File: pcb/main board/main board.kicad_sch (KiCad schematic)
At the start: 33 parts, among them J10 12V Battery, J11 BAU, J12 Servo 4 Conn, J13 Servo 1 Conn, J14 Servo 2 Conn, J15 Servo 3 Conn, J16 Servo 5 Conn, J17 Servo 6 Conn, J5 I2C 0 Conn, J6 I2C 1 Conn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

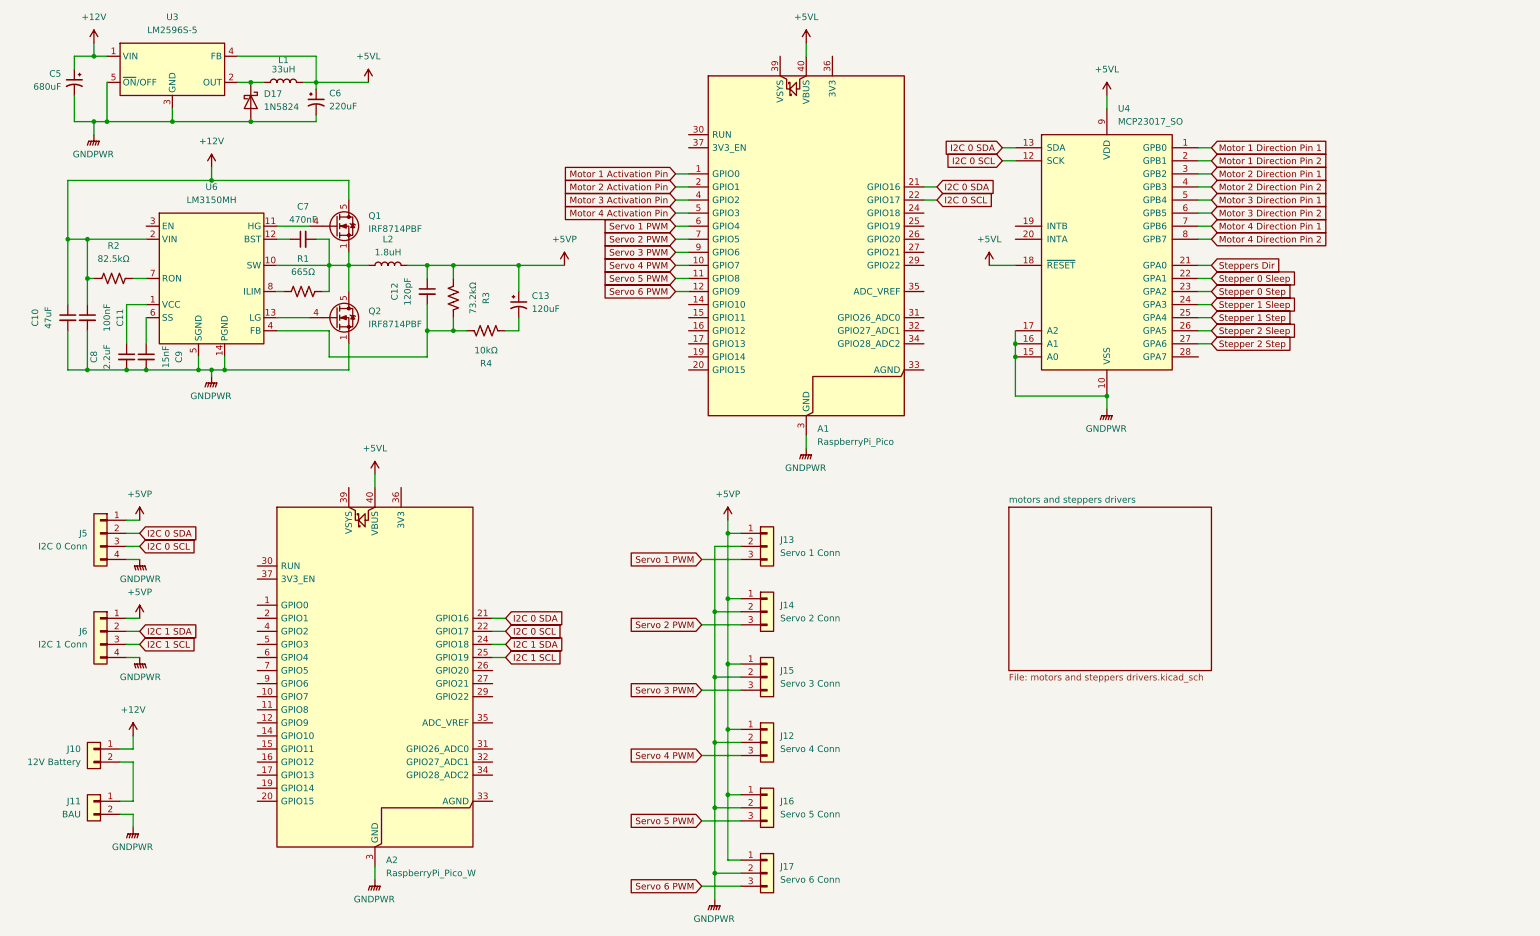
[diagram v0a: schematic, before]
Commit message: Modified LM2596S to be a module.
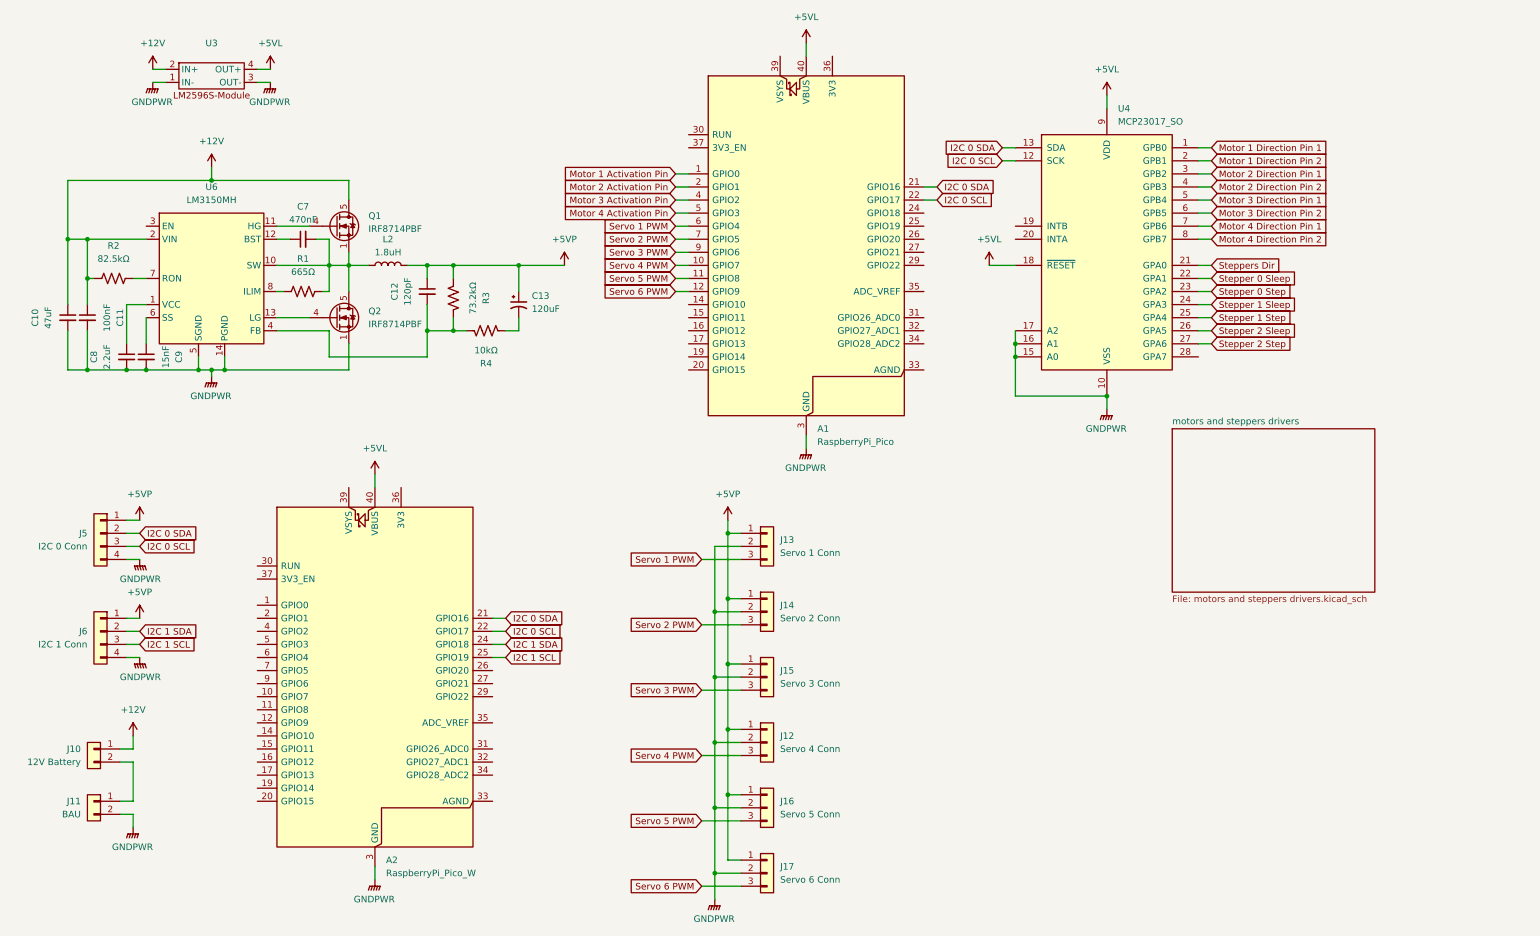
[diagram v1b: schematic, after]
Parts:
- removed C5: 680uF, symbol Device:C_Polarized_Small_US
- removed C6: 220uF, symbol Device:C_Polarized_Small_US
- removed D17: 1N5824, Diode_THT:D_DO-201AD_P15.24mm_Horizontal, symbol Diode:1N5822
- removed L1: 33uH, symbol Device:L
- removed U3: LM2596S-5, Package_TO_SOT_SMD:TO-263-5_TabPin3, symbol Regulator_Switching:LM2596S-5
- added U3: ~, LM2596S-Module:LM2596S-Module, symbol LM2596S-Module:LM2596S-Module
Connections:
- net +12V: now also U3.2 (IN+)
- net +5VL: now also U3.4 (OUT+)
- net GNDPWR: now also U3.1 (IN-), U3.3 (OUT-)

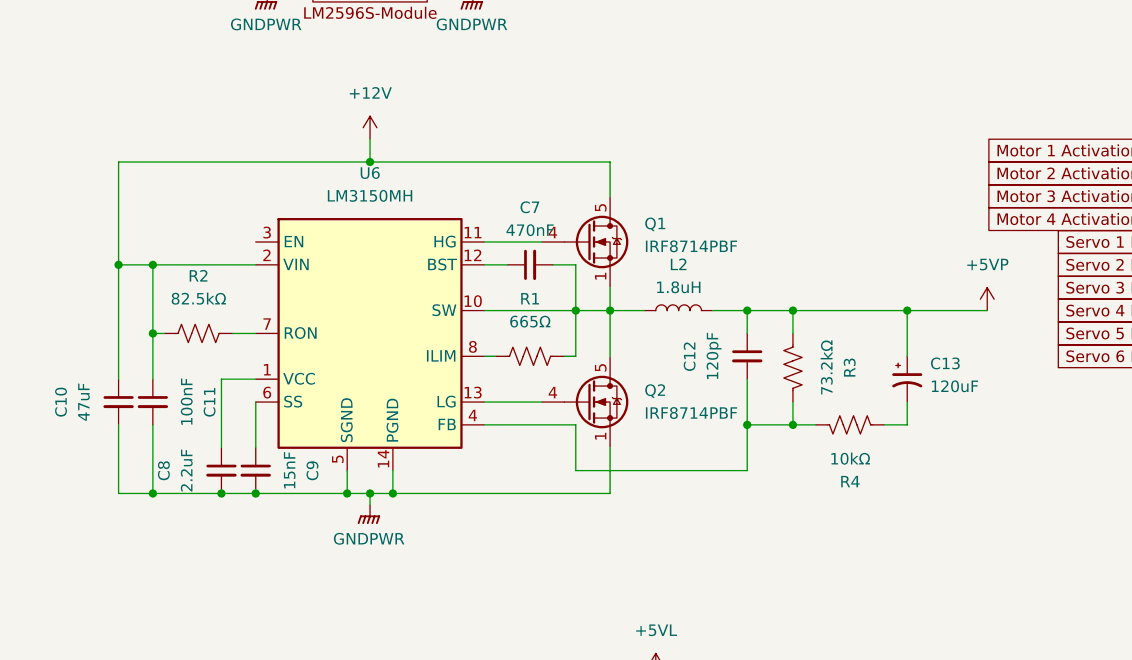
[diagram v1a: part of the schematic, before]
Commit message: Changed some capacitors and assigned every component.
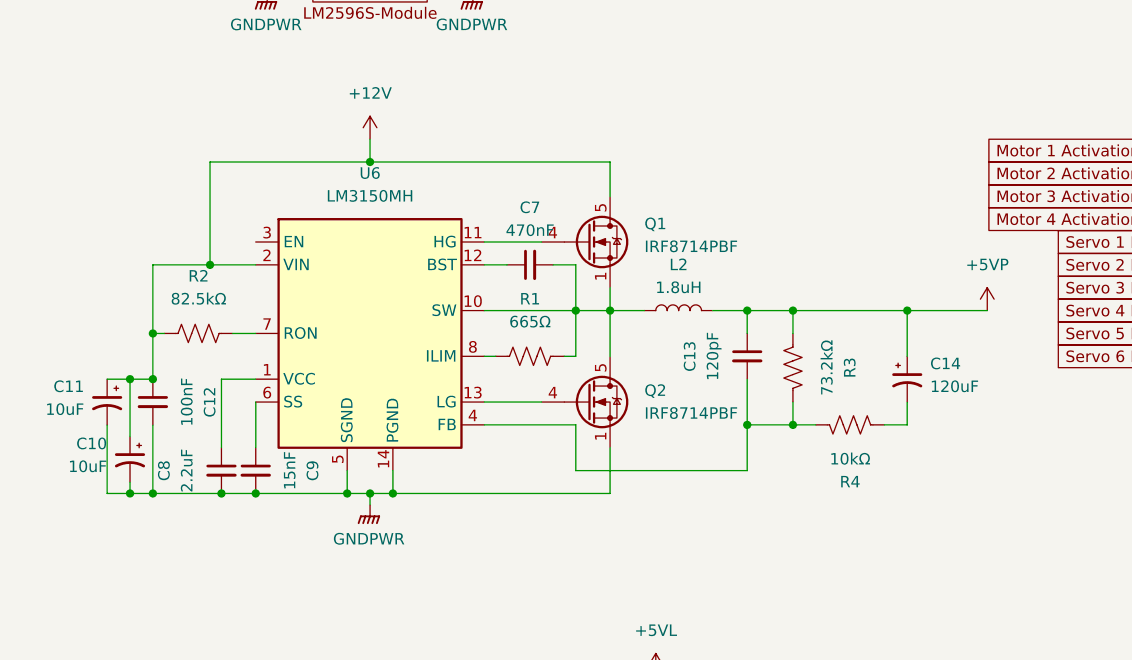
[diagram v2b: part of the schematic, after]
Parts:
- removed C10: 47uF, symbol Device:C_Small
- added C10, C11: 10uF, Capacitor_THT:CP_Radial_D5.0mm_P2.50mm, symbol Device:C_Polarized_Small_US
- C12: renamed from C11; footprint (none) -> Capacitor_THT:C_Disc_D4.3mm_W1.9mm_P5.00mm
- C13: renamed from C12; footprint (none) -> Capacitor_THT:C_Disc_D4.3mm_W1.9mm_P5.00mm
- C14: renamed from C13; footprint (none) -> Capacitor_THT:CP_Radial_D10.0mm_P5.00mm
- C7, C8, C9: footprint (none) -> Capacitor_THT:C_Disc_D4.3mm_W1.9mm_P5.00mm
- J10, J11: footprint (none) -> Connector:JWT_A3963_1x02_P3.96mm_Vertical
- J12, J13, J14, J15, J16, J17: footprint (none) -> Connector:FanPinHeader_1x03_P2.54mm_Vertical
- J5, J6: footprint (none) -> Connector:FanPinHeader_1x04_P2.54mm_Vertical
- L2: footprint (none) -> Inductor_SMD:L_APV_APH1040
- R1, R2, R3, R4: footprint (none) -> Resistor_THT:R_Axial_DIN0207_L6.3mm_D2.5mm_P10.16mm_Horizontal
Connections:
- net +12V: now also C10.1, C11.1
- net GNDPWR: now also C10.2, C11.2

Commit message: Started Motors Wiring
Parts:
- A2: footprint Module:RaspberryPi_Pico_W_SMD_HandSolder -> Module:RaspberryPi_Pico_Common_Unspecified
- J10, J11: footprint Connector:JWT_A3963_1x02_P3.96mm_Vertical -> Connector_PinHeader_2.54mm:PinHeader_1x02_P2.54mm_Vertical
- J12, J13, J14, J15, J16, J17: footprint Connector:FanPinHeader_1x03_P2.54mm_Vertical -> Connector_PinHeader_2.54mm:PinHeader_1x03_P2.54mm_Vertical
- J5, J6: footprint Connector:FanPinHeader_1x04_P2.54mm_Vertical -> Connector_PinHeader_2.54mm:PinHeader_1x04_P2.54mm_Vertical
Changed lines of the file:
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@@
 			)
 		)
-		(property "Footprint" "Connector:FanPinHeader_1x03_P2.54mm_Vertical"
+		(property "Footprint" "Connector_PinHeader_2.54mm:PinHeader_1x03_P2.54mm_Vertical"
 			(at 158.75 130.81 0)
 			(effects
@@
 			)
 		)
-		(property "Footprint" "Connector:JWT_A3963_1x02_P3.96mm_Vertical"
+		(property "Footprint" "Connector_PinHeader_2.54mm:PinHeader_1x02_P2.54mm_Vertical"
 			(at 27.94 157.48 0)
 			(effects
@@
 			)
 		)
-		(property "Footprint" "Connector:FanPinHeader_1x04_P2.54mm_Vertical"
+		(property "Footprint" "Connector_PinHeader_2.54mm:PinHeader_1x04_P2.54mm_Vertical"
 			(at 29.21 134.62 0)
 			(effects
@@
 			)
 		)
-		(property "Footprint" "Connector:JWT_A3963_1x02_P3.96mm_Vertical"
+		(property "Footprint" "Connector_PinHeader_2.54mm:PinHeader_1x02_P2.54mm_Vertical"
 			(at 27.94 167.64 0)
 			(effects
@@
 			)
 		)
-		(property "Footprint" "Connector:FanPinHeader_1x03_P2.54mm_Vertical"
+		(property "Footprint" "Connector_PinHeader_2.54mm:PinHeader_1x03_P2.54mm_Vertical"
 			(at 158.75 168.91 0)
 			(effects
@@
 			)
 		)
-		(property "Footprint" "Connector:FanPinHeader_1x04_P2.54mm_Vertical"
+		(property "Footprint" "Connector_PinHeader_2.54mm:PinHeader_1x04_P2.54mm_Vertical"
 			(at 29.21 115.57 0)
 			(effects
@@
 			)
 		)
-		(property "Footprint" "Connector:FanPinHeader_1x03_P2.54mm_Vertical"
+		(property "Footprint" "Connector_PinHeader_2.54mm:PinHeader_1x03_P2.54mm_Vertical"
 			(at 158.75 118.11 0)
 			(effects
@@
 			)
 		)
-		(property "Footprint" "Connector:FanPinHeader_1x03_P2.54mm_Vertical"
+		(property "Footprint" "Connector_PinHeader_2.54mm:PinHeader_1x03_P2.54mm_Vertical"
 			(at 158.75 143.51 0)
 			(effects
@@
 			)
 		)
-		(property "Footprint" "Module:RaspberryPi_Pico_W_SMD_HandSolder"
+		(property "Footprint" "Module:RaspberryPi_Pico_Common_Unspecified"
 			(at 82.55 191.77 0)
 			(effects
@@
 			)
 		)
-		(property "Footprint" "Connector:FanPinHeader_1x03_P2.54mm_Vertical"
+		(property "Footprint" "Connector_PinHeader_2.54mm:PinHeader_1x03_P2.54mm_Vertical"
 			(at 158.75 181.61 0)
 			(effects
@@
 			)
 		)
-		(property "Footprint" "Connector:FanPinHeader_1x03_P2.54mm_Vertical"
+		(property "Footprint" "Connector_PinHeader_2.54mm:PinHeader_1x03_P2.54mm_Vertical"
 			(at 158.75 156.21 0)
 			(effects

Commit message: Finished DC motors wiring aand started 5VP regulator.
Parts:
- C14: footprint Capacitor_THT:CP_Radial_D10.0mm_P5.00mm -> Capacitor_THT:CP_Radial_D6.3mm_P2.50mm
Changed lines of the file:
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@@
 			)
 		)
-		(property "Footprint" "Capacitor_THT:CP_Radial_D10.0mm_P5.00mm"
+		(property "Footprint" "Capacitor_THT:CP_Radial_D6.3mm_P2.50mm"
 			(at 110.49 71.12 0)
 			(effects

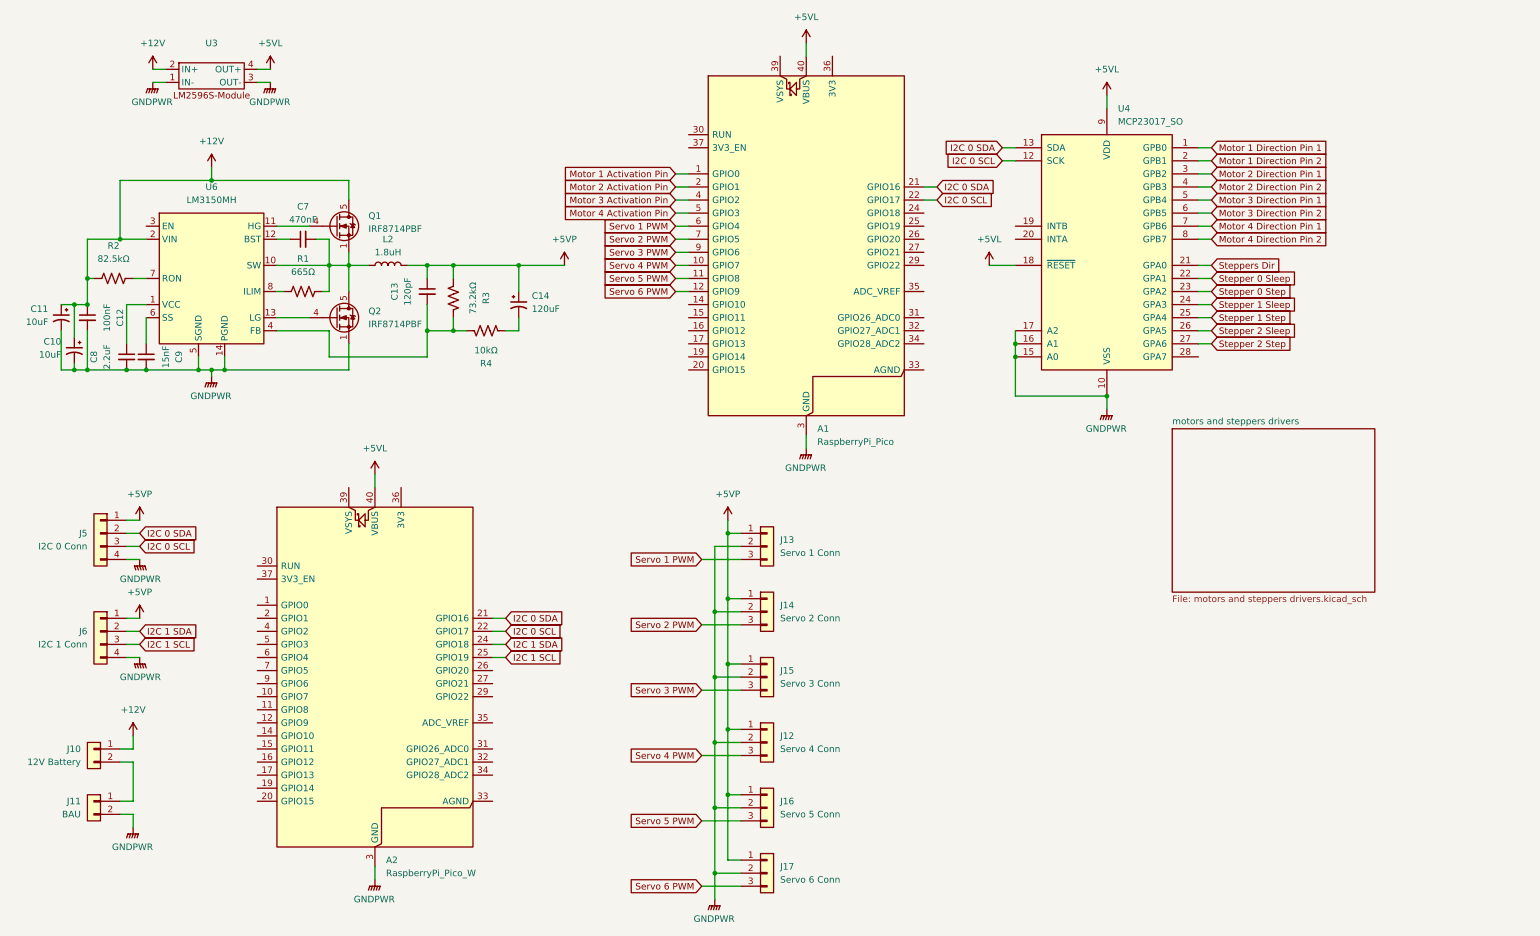
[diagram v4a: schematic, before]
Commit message: Rearanged board
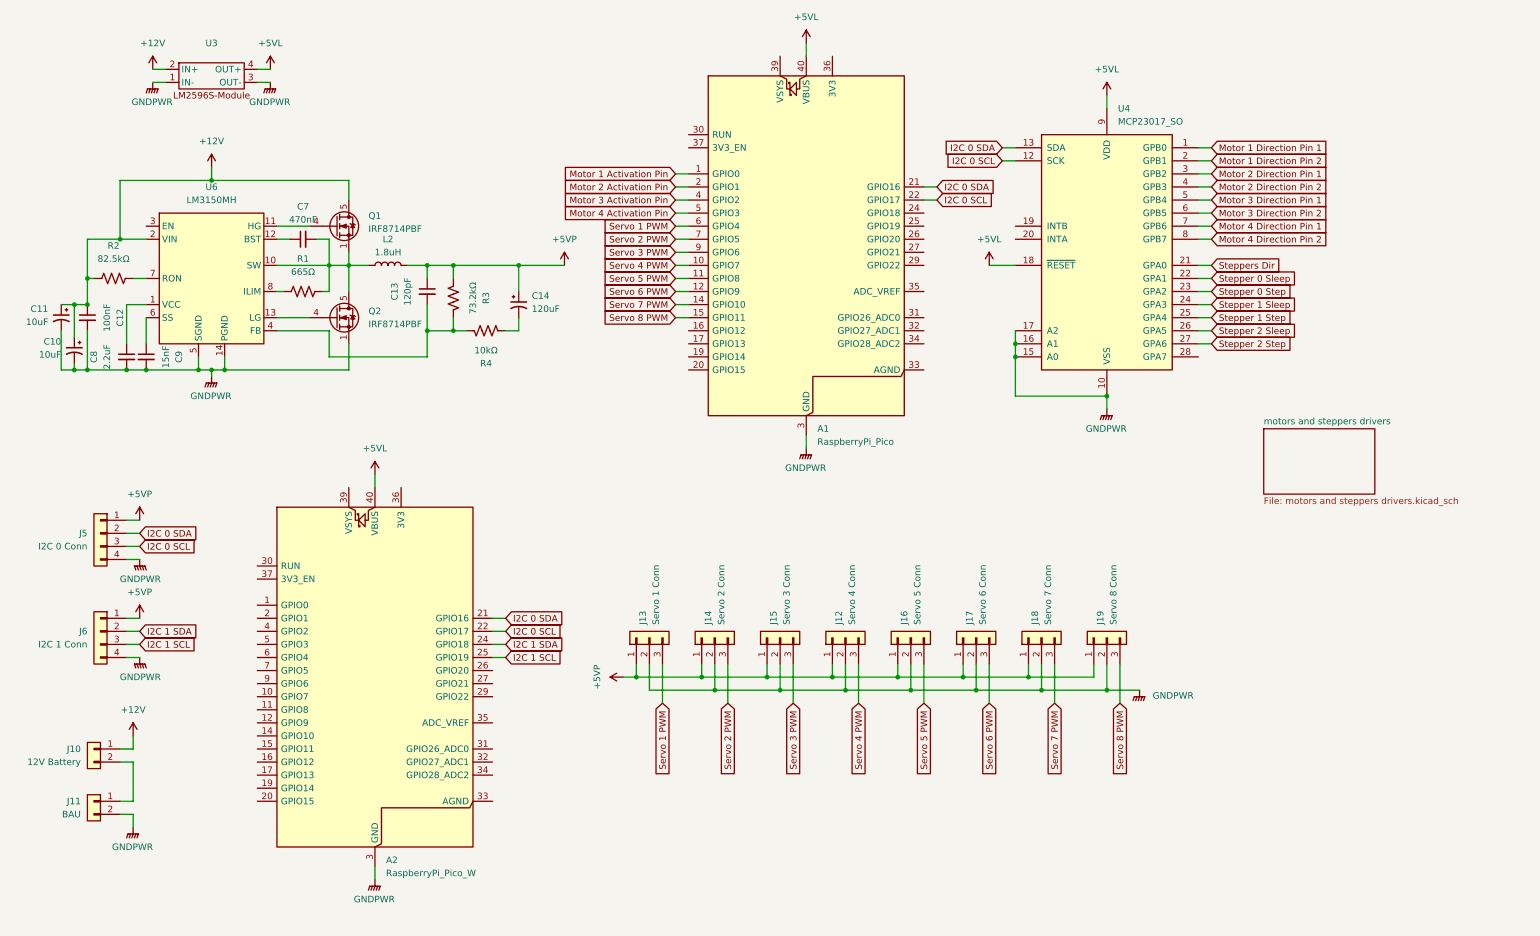
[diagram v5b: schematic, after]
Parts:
- added J18: Servo 7 Conn, Connector_PinHeader_2.54mm:PinHeader_1x03_P2.54mm_Vertical, symbol Connector_Generic:Conn_01x03
- added J19: Servo 8 Conn, Connector_PinHeader_2.54mm:PinHeader_1x03_P2.54mm_Vertical, symbol Connector_Generic:Conn_01x03
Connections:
- net +5VP: now also J18.1 (Pin_1), J19.1 (Pin_1)
- net GNDPWR: now also J18.2 (Pin_2), J19.2 (Pin_2)
- net Servo 7 PWM: now reaches A1.14 (GPIO10)
- net Servo 7 PWM: now also J18.3 (Pin_3)
- net Servo 8 PWM: now reaches A1.15 (GPIO11)
- net Servo 8 PWM: now also J19.3 (Pin_3)
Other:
- moved on the sheet: J12, J13, J14, J15, J16, J17
